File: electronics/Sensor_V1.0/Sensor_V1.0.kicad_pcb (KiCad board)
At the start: 2 copper layers, 45.9 x 25.6 mm, 53 parts, among them J1 nuclone_small_left, J2 nuclone_small_right, J5 DevBoardUartInput, Q1 BC846, U1 PPG_sensor, U2 reference_sot23-3

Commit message: WIP comparator section and final fixes for ERC
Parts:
- added C10: 1u, SquantorRcl:C_0603, B.Cu at (99.9, 92.7)
- added R15: R, SquantorRcl:R_0603_hand, B.Cu at (96.9, 96.7)
- added R16: R, SquantorRcl:R_0603_hand, B.Cu at (94.7, 95.1)
- added R17: R, SquantorRcl:R_0603_hand, B.Cu at (94.7, 92.2)
- added R18: R, SquantorRcl:R_0603_hand, B.Cu at (96.9, 90.5)
- added TP13: Cmp Out, SquantorTestPoints:TestPoint_hole_H03R05, F.Cu at (99.9, 95.0)
- added U3: MCP6541, SquantorIC:SOT23-5-Microchip-OT, B.Cu at (97.3, 93.6)
- N1, N2, N3: moved to F.Cu
- moved N3 9.03 mm to (84.3, 97.5), turned to 0 degrees
- moved N1 7.44 mm to (85.1, 91.5), turned to 0 degrees
- moved N2 4.46 mm to (86.6, 95.5), turned to 180 degrees
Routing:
- net /LED2: track 12.6 -> 10.5 mm

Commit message: added resistor network decoupling capacitpr
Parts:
- removed R14: R, SquantorRcl:R_0603_hand
- added C11: 1u, SquantorRcl:C_0603, B.Cu at (107.3, 62.4)
- N2: value 20200808 -> 20200810
- moved C8 1.70 mm to (79.5, 86.7)
- moved C9 1.70 mm to (83.3, 86.7)
- moved Q1 1.70 mm to (86.1, 86.7)
- moved R11 1.70 mm to (90.2, 87.5)
- moved R8 1.70 mm to (88.7, 87.5)
- moved C7 1.70 mm to (81.4, 86.7)
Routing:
- net /PD_OUT_GUARD: track 25.6 -> 17.6 mm

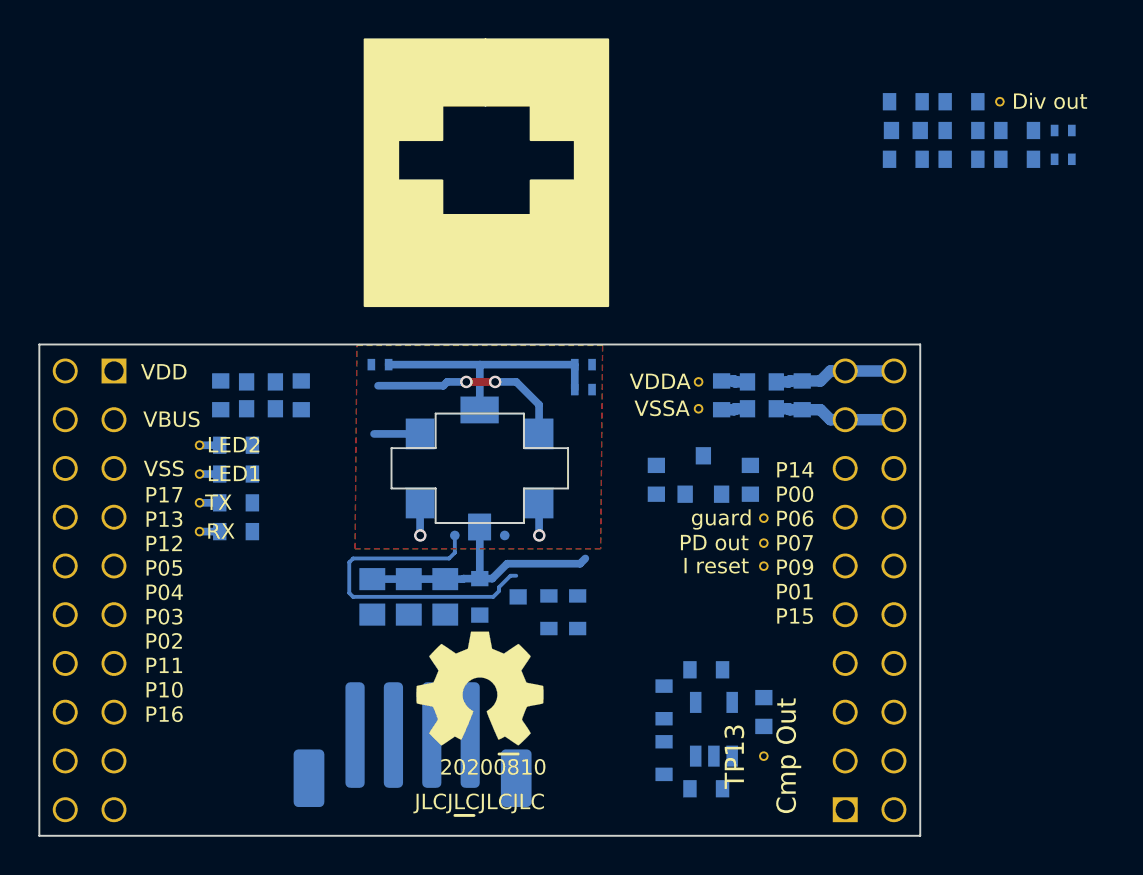
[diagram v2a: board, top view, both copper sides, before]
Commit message: added ground plane(s)
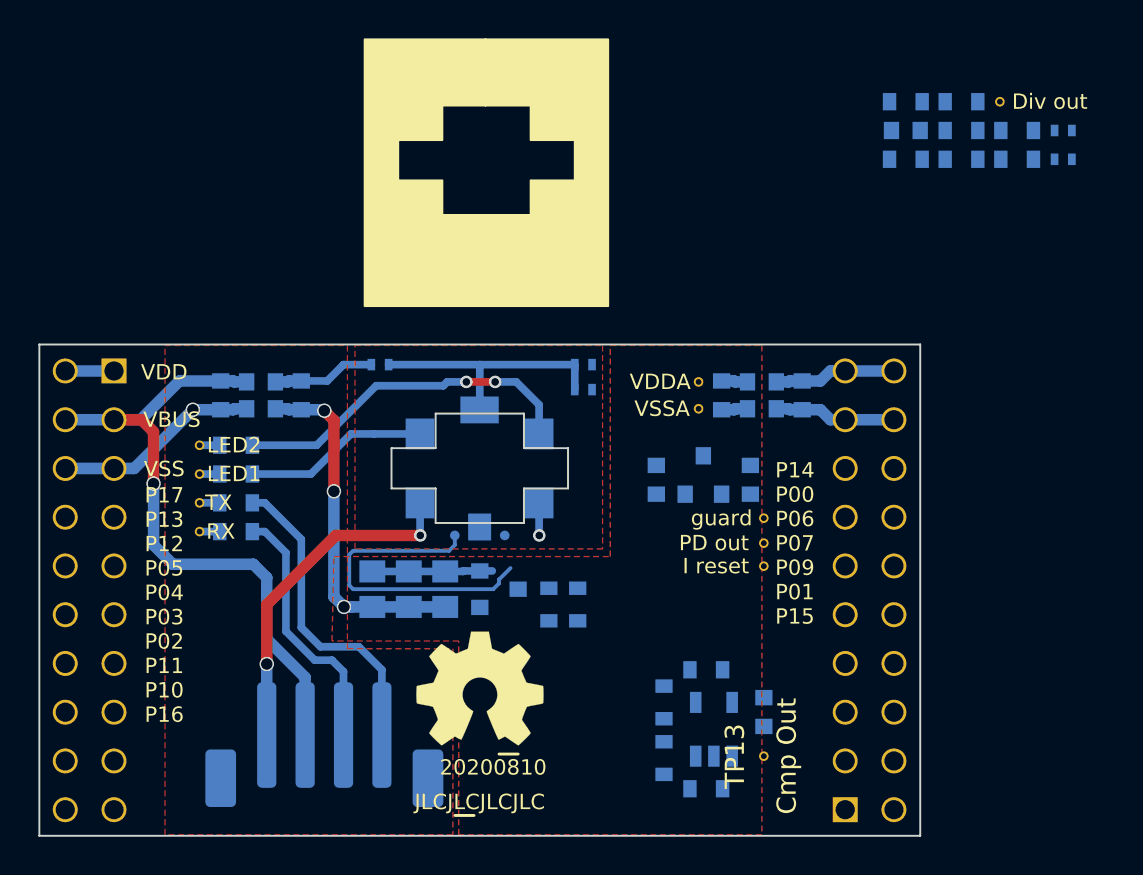
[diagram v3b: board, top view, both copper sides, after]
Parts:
- moved J5 4.60 mm to (77.0, 94.4)
- moved C7 0.40 mm to (81.4, 86.3)
- moved C8 0.40 mm to (79.5, 86.3)
- moved C9 0.40 mm to (83.3, 86.3)
- moved Q1 0.40 mm to (86.1, 86.3)
- moved R11 0.40 mm to (90.2, 87.1)
- moved R8 0.40 mm to (88.7, 87.1)
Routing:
- net /VBUS: track 0.00 -> 34.2 mm, vias 0 -> 1
- net /VSS: track 3.39 -> 30.4 mm, vias 2 -> 4
- net /VSSA: track 1.37 -> 19.9 mm, vias 0 -> 3
- net Net-(J5-Pad4): track 0.00 -> 16.4 mm
- net Net-(J5-Pad3): track 0.00 -> 13.5 mm
- net /LED2: track 10.5 -> 18.3 mm
- net /PD_OUT: track 14.3 -> 6.52 mm
- net /LED1: track 2.40 -> 9.61 mm
- net Net-(C4-Pad1): track 0.00 -> 5.37 mm
- net /VDD: track 0.00 -> 2.54 mm
- net /PD_OUT_GUARD: track 17.6 -> 16.9 mm
- added copper zone on F.Cu, net /VSSA

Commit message: updated some more placement
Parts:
- moved C11 37.8 mm to (90.3, 96.2)
- moved JP4 37.8 mm to (98.5, 97.7)
- moved JP5 37.8 mm to (98.5, 96.2)
- moved R10 37.8 mm to (93.2, 97.7)
- moved R12 37.8 mm to (90.3, 94.7)
- moved R13 37.8 mm to (90.3, 97.7)
- moved R5 37.8 mm to (96.1, 96.2)
- moved R6 37.8 mm to (96.1, 97.7)
- moved R7 37.8 mm to (93.2, 94.7)
- moved R9 37.8 mm to (93.2, 96.2)
- moved TP11 37.8 mm to (95.2, 94.7)
- moved C10 3.61 mm to (99.7, 89.1)
- moved R15 3.61 mm to (96.7, 93.1)
- moved R17 3.61 mm to (94.5, 88.6)
- moved R16 3.61 mm to (94.5, 91.5)
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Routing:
- net /VSSA: track 19.9 -> 35.2 mm, vias 3 -> 5
- net /VDDA: track 1.37 -> 15.8 mm, vias 0 -> 2
- net /PD_OUT: track 6.52 -> 12.7 mm
- net Net-(Q1-Pad1): track 0.00 -> 5.39 mm
- net /VREF: track 0.00 -> 1.50 mm
- net /VSS: track 30.4 -> 29.8 mm

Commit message: WIP layout
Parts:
- removed R10, R13, R5, R6, R9: R, SquantorRcl:R_0603_hand
- moved R15 8.68 mm to (92.5, 85.5), turned to 90 degrees
- moved TP12 6.40 mm to (91.8, 87.9)
- moved R16 5.00 mm to (94.7, 86.5), turned to 0 degrees
- moved TP13 4.92 mm to (94.8, 91.8), turned to 0 degrees
- moved R12 3.96 mm to (93.2, 97.4)
- moved R7 3.96 mm to (96.1, 97.4)
- moved R17 3.74 mm to (97.6, 86.5), turned to 0 degrees
- moved C10 3.68 mm to (97.1, 91.7), turned to 180 degrees
- moved R18 3.16 mm to (99.3, 88.7), turned to 90 degrees
- moved C11 2.92 mm to (93.2, 95.9)
- moved U3 1.27 mm to (96.2, 89.1), turned to 90 degrees
- moved TP11 1.20 mm to (95.2, 95.9)
- moved TP10 1.00 mm to (96.8, 84.6)
- moved TP9 1.00 mm to (96.8, 83.3)
- moved JP4 0.20 mm to (98.5, 97.5)
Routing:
- net /PD_OUT_GUARD: track 17.2 -> 29.1 mm
- net /VREF: track 1.50 -> 9.05 mm
- net /VDDA: track 15.8 -> 22.6 mm
- net /PD_OUT: track 12.7 -> 15.7 mm
- net /VSSA: track 35.2 -> 37.5 mm, vias 5 -> 6

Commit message: routing completed
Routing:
- net /VSSA: track 37.5 -> 68.5 mm, vias 6 -> 9
- net /VREF: track 9.05 -> 35.8 mm, vias 0 -> 2
- net /VDDA: track 22.6 -> 47.8 mm, vias 2 -> 4
- net /Divider_out: track 0.00 -> 18.4 mm
- net /PD_OUT_GUARD: track 29.1 -> 42.2 mm
- net /CMP_OUT: track 0.00 -> 8.17 mm
- net /PD_OUT: track 15.7 -> 20.0 mm
- net Net-(R15-Pad1): track 0.00 -> 3.89 mm
- net Net-(R17-Pad2): track 0.00 -> 3.85 mm
- net /I_reset: track 0.00 -> 2.69 mm
- net Net-(JP4-Pad2): track 0.00 -> 2.44 mm

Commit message: more silk placements
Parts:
- moved TP12 1.21 mm to (91.3, 89.0)
- moved N2 1.17 mm to (86.0, 96.5)
- moved N1 1.01 mm to (85.0, 92.5)
- moved N3 0.51 mm to (84.3, 98.0)
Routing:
- net /I_reset: track 2.69 -> 3.59 mm
